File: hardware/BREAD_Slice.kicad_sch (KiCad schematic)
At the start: 15 parts, among them J1 Conn_01x10_Female, U1 AP63205

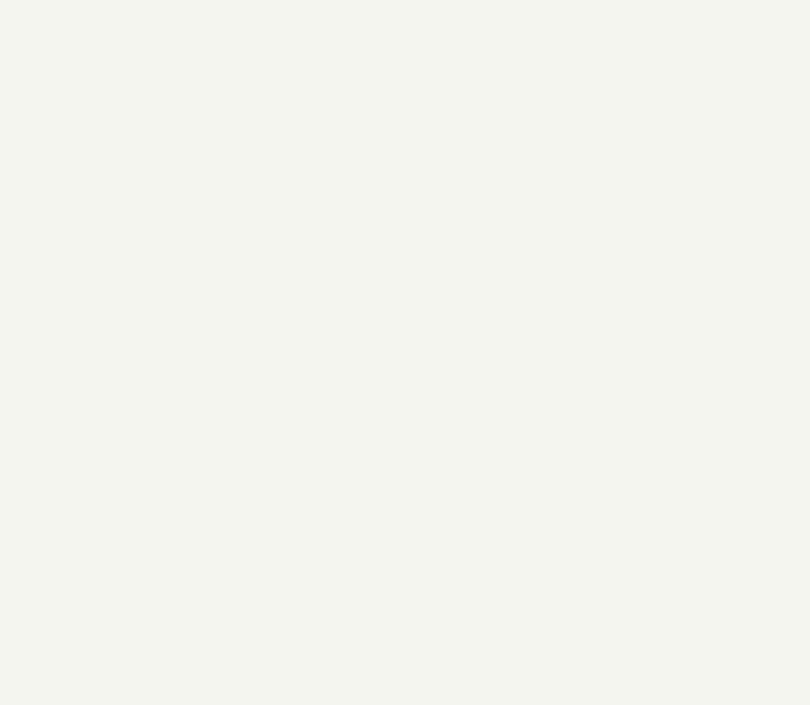
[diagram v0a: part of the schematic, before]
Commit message: initial commit, max31865 sub sheet done
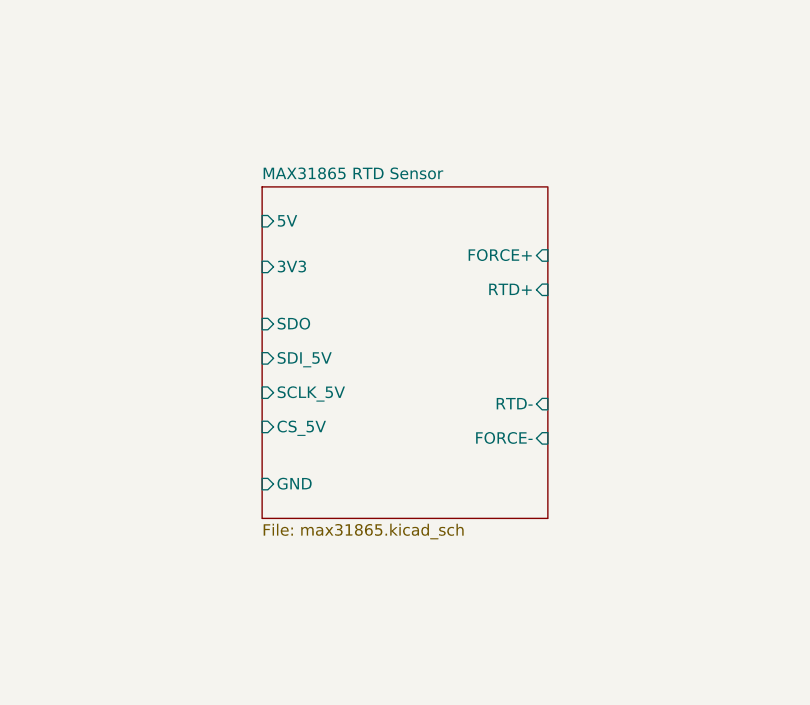
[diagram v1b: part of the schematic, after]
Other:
- added sheet MAX31865 RTD Sensor (max31865.kicad_sch)
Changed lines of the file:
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@@
 		(on_board yes)
 		(dnp no)
-		(property "Reference" "#FLG02"
+		(property "Reference" "#FLG03"
 			(at 48.895 49.53 0)
 			(effects
@@
 			(project "BREAD_Slice"
 				(path "/66043bca-a260-4915-9fce-8a51d324c687"
-					(reference "#FLG02")
+					(reference "#FLG03")
 					(unit 1)
 				)
@@
 		(on_board yes)
 		(dnp no)
-		(property "Reference" "#FLG01"
+		(property "Reference" "#FLG02"
 			(at 47.625 27.94 0)
 			(effects
@@
 			(project "BREAD_Slice"
 				(path "/66043bca-a260-4915-9fce-8a51d324c687"
-					(reference "#FLG01")
+					(reference "#FLG02")
 					(unit 1)
 				)
@@
 		(on_board yes)
 		(dnp no)
-		(property "Reference" "#PWR04"
+		(property "Reference" "#PWR02"
 			(at 26.67 95.25 0)
 			(effects
@@
 			(project "BREAD_Slice"
 				(path "/66043bca-a260-4915-9fce-8a51d324c687"
-					(reference "#PWR04")
+					(reference "#PWR02")
 					(unit 1)
 				)
@@
 		(on_board yes)
 		(dnp no)
-		(property "Reference" "#PWR02"
+		(property "Reference" "#PWR012"
 			(at 55.88 73.66 0)
 			(effects
@@
 			(project ""
 				(path "/66043bca-a260-4915-9fce-8a51d324c687"
-					(reference "#PWR02")
+					(reference "#PWR012")
 					(unit 1)
 				)
@@
 		(dnp no)
 		(fields_autoplaced yes)
-		(property "Reference" "#PWR05"
+		(property "Reference" "#PWR07"
 			(at 44.45 105.41 0)
 			(effects
@@
 			(project "BREAD_Slice"
 				(path "/66043bca-a260-4915-9fce-8a51d324c687"
-					(reference "#PWR05")
+					(reference "#PWR07")
 					(unit 1)
 				)
@@
 		(on_board yes)
 		(dnp no)
-		(property "Reference" "#PWR012"
+		(property "Reference" "#PWR08"
 			(at 45.72 119.38 0)
 			(effects
@@
 			(project "BREAD_Slice"
 				(path "/66043bca-a260-4915-9fce-8a51d324c687"
-					(reference "#PWR012")
+					(reference "#PWR08")
 					(unit 1)
 				)
@@
 		(on_board yes)
 		(dnp no)
-		(property "Reference" "#PWR08"
+		(property "Reference" "#PWR04"
 			(at 30.48 55.88 0)
 			(effects
@@
 			(project "BREAD_Slice"
 				(path "/66043bca-a260-4915-9fce-8a51d324c687"
-					(reference "#PWR08")
+					(reference "#PWR04")
 					(unit 1)
 				)
@@
 		(on_board yes)
 		(dnp no)
-		(property "Reference" "#PWR03"
+		(property "Reference" "#PWR09"
 			(at 46.99 95.25 0)
 			(effects
@@
 			(project ""
 				(path "/66043bca-a260-4915-9fce-8a51d324c687"
-					(reference "#PWR03")
+					(reference "#PWR09")
 					(unit 1)
 				)
@@
 		(on_board yes)
 		(dnp no)
-		(property "Reference" "#PWR09"
+		(property "Reference" "#PWR03"
 			(at 30.48 35.56 0)
 			(effects
@@
 			(project "BREAD_Slice"
 				(path "/66043bca-a260-4915-9fce-8a51d324c687"
-					(reference "#PWR09")
+					(reference "#PWR03")
 					(unit 1)
 				)
@@
 		(on_board yes)
 		(dnp no)
-		(property "Reference" "#FLG03"
+		(property "Reference" "#FLG01"
 			(at 28.575 100.33 0)
 			(effects
@@
 			(project "BREAD_Slice"
 				(path "/66043bca-a260-4915-9fce-8a51d324c687"
-					(reference "#FLG03")
+					(reference "#FLG01")
 					(unit 1)
 				)
@@
 		(on_board yes)
 		(dnp no)
-		(property "Reference" "#PWR07"
+		(property "Reference" "#PWR05"
 			(at 31.75 106.68 0)
 			(effects
@@
 			(project "BREAD_Slice"
 				(path "/66043bca-a260-4915-9fce-8a51d324c687"
-					(reference "#PWR07")
+					(reference "#PWR05")
 					(unit 1)
 				)
@@
 				)
 			)
+		)
+	)
+	(sheet
+		(at 123.19 55.88)
+		(size 31.75 36.83)
+		(exclude_from_sim no)
+		(in_bom yes)
+		(on_board yes)
+		(dnp no)
+		(fields_autoplaced yes)
+		(stroke
+			(width 0.1524)
+			(type solid)
+		)
+		(fill
+			(color 0 0 0 0.0000)
+		)
+		(property "Sheetname" "MAX31865 RTD Sensor"
+			(at 123.19 55.1684 0)
+			(effects
+				(font
+					(size 1.27 1.27)
+				)
+				(justify left bottom)
+			)
+		)
+		(property "Sheetfile" "max31865.kicad_sch"
+			(at 123.19 93.2946 0)
+			(effects
+				(font
+					(size 1.27 1.27)
+				)
+				(justify left top)
+			)
+		)
+		(pin "3V3" input
+			(at 123.19 64.77 180)
+			(effects
+				(font
+					(size 1.27 1.27)
+				)
+				(justify left)
+			)
+		)
+		(pin "5V" input
+			(at 123.19 59.69 180)
+			(effects
+				(font
+					(size 1.27 1.27)
+				)
+				(justify left)
+			)
+		)
+		(pin "CS_5V" input
+			(at 123.19 82.55 180)
+			(effects
+				(font
+					(size 1.27 1.27)
+				)
+				(justify left)
+			)
+		)
+		(pin "FORCE+" input
+			(at 154.94 63.5 0)
+			(effects
+				(font
+					(size 1.27 1.27)
+				)
+				(justify right)
+			)
+		)
+		(pin "FORCE-" input
+			(at 154.94 83.82 0)
+			(effects
+				(font
+					(size 1.27 1.27)
+				)
+				(justify right)
+			)
+		)
+		(pin "RTD+" input
+			(at 154.94 67.31 0)
+			(effects
+				(font
+					(size 1.27 1.27)
+				)
+				(justify right)
+			)
+		)
+		(pin "RTD-" input
+			(at 154.94 80.01 0)
+			(effects
+				(font
+					(size 1.27 1.27)
+				)
+				(justify right)
+			)
+		)
+		(pin "SCLK_5V" input
+			(at 123.19 78.74 180)
+			(effects
+				(font
+					(size 1.27 1.27)
+				)
+				(justify left)
+			)
+		)
+		(pin "SDI_5V" input
+			(at 123.19 74.93 180)
+			(effects
+				(font
+					(size 1.27 1.27)
+				)
+				(justify left)
+			)
+		)
+		(pin "SDO" input
+			(at 123.19 71.12 180)
+			(effects
+				(font
+					(size 1.27 1.27)
+				)
+				(justify left)
+			)
+		)
+		(pin "GND" input
+			(at 123.19 88.9 180)
+			(effects
+				(font
+					(size 1.27 1.27)
+				)
+				(justify left)
+			)
+		)
+		(instances
+			(project "BREAD_Slice"
+				(path "/66043bca-a260-4915-9fce-8a51d324c687"
+					(page "2")
+				)
+			)

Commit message: initial commit, complete schematic and board
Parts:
- added J2, J3, J4, J5, J6, J7, J8, J9: Screw_Terminal_01x02, TerminalBlock_4Ucon:TerminalBlock_4Ucon_1x02_P3.50mm_Horizontal, symbol Connector:Screw_Terminal_01x02
- added R1: 10k, Resistor_SMD:R_0805_2012Metric_Pad1.20x1.40mm_HandSolder, symbol Device:R
- added U2: TXB0108PW, Package_SO:TSSOP-20_4.4x6.5mm_P0.65mm, symbol Logic_LevelTranslator:TXB0108PW
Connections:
- net +5V: now also R1.1, U2.2 (V_{CCA})
- net GND: now also U2.1 (A1), U2.11 (GND)
- net MAX31865 RTD Sensor1/FORCE+: now also J2.2 (Pin_2)
- net MAX31865 RTD Sensor1/FORCE-: now also J3.1 (Pin_1)
- net MAX31865 RTD Sensor1/RTD+: now also J2.1 (Pin_1)
- net MAX31865 RTD Sensor1/RTD-: now also J3.2 (Pin_2)
- net CS4: now reaches A1.10 (D7)
- net CS4: now also U2.3 (A2)
- net CS3: now reaches A1.11 (D8)
- net CS3: now also U2.4 (A3)
- net CS2: now reaches A1.12 (D9)
- net CS2: now also U2.5 (A4)
- net CS1: now reaches A1.13 (D10)
- net CS1: now also U2.6 (A5)
- net MOSI: now reaches A1.14 (D11)
- net MOSI: now also U2.7 (A6)
- net MISO: now reaches A1.15 (D12)
- net MISO: now also U2.8 (A7)
- net SCK: now reaches A1.16 (D13)
- net SCK: now also U2.9 (A8)
- net +3.3V: now reaches A1.17 (3V3)
- net +3.3V: now also U2.19 (V_{CCB})
- net DRDY1: now reaches A1.19 (A0)
- net DRDY2: now reaches A1.20 (A1)
- net DRDY4: now reaches A1.21 (A2)
- net DRDY3: now reaches A1.22 (A3)
- new net: R1.2, U2.10 (OE)
- new net CS1_3V: U2.15 (B5)
- new net CS2_3V: U2.16 (B4)
- new net CS3_3V: U2.17 (B3)
- new net CS4_3V: U2.18 (B2)
- new net MAX31865 RTD Sensor2/FORCE+: J4.2 (Pin_2)
- new net MAX31865 RTD Sensor2/FORCE-: J5.1 (Pin_1)
- new net MAX31865 RTD Sensor2/RTD+: J4.1 (Pin_1)
- new net MAX31865 RTD Sensor2/RTD-: J5.2 (Pin_2)
- new net MAX31865 RTD Sensor3/FORCE+: J6.2 (Pin_2)
- new net MAX31865 RTD Sensor3/FORCE-: J7.1 (Pin_1)
- new net MAX31865 RTD Sensor3/RTD+: J6.1 (Pin_1)
- new net MAX31865 RTD Sensor3/RTD-: J7.2 (Pin_2)
- new net MAX31865 RTD Sensor4/FORCE+: J8.2 (Pin_2)
- new net MAX31865 RTD Sensor4/FORCE-: J9.1 (Pin_1)
- new net MAX31865 RTD Sensor4/RTD+: J8.1 (Pin_1)
- new net MAX31865 RTD Sensor4/RTD-: J9.2 (Pin_2)
- new net MISO_3V: U2.13 (B7)
- new net MOSI_3V: U2.14 (B6)
- new net SCK_3V: U2.12 (B8)
- no-connect marks 22 -> 11
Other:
- sheet MAX31865 RTD Sensor renamed MAX31865 RTD Sensor1
- added sheet MAX31865 RTD Sensor2 (max31865.kicad_sch)
- added sheet MAX31865 RTD Sensor3 (max31865.kicad_sch)
- added sheet MAX31865 RTD Sensor4 (max31865.kicad_sch)
- sheet MAX31865 RTD Sensor1 ports: added CS, DRDY, SCLK, SDI; removed 5V, CS_5V, SCLK_5V, SDI_5V

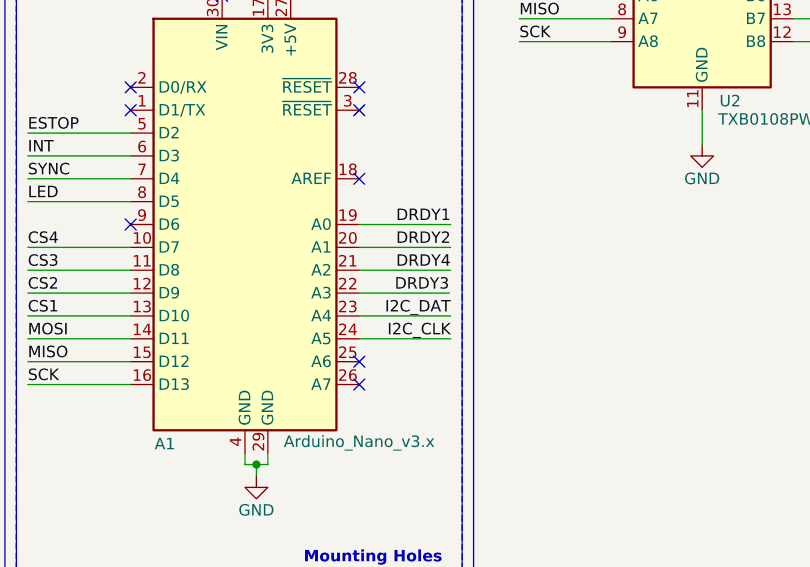
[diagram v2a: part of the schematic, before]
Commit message: review and revise board to use kmlib properly and clear drc/erc
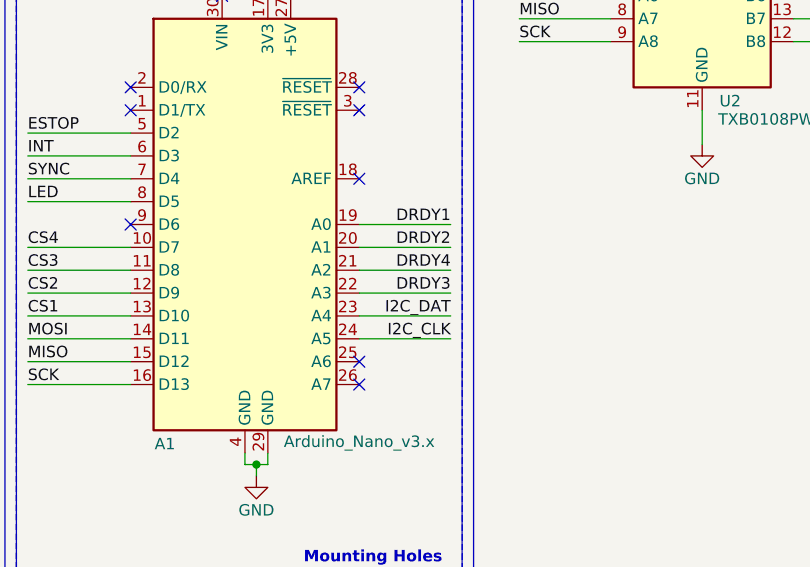
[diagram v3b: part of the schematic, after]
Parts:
- A1: footprint Module:Arduino_Nano -> KMLib_Boards_Modules:Arduino_Nano_Headers
- D1: footprint SparkFun-LED:WS2812-5050-4PIN -> KMLib_IC_SMD:WS2812-5050-4PIN; symbol SparkFun-LED:WS2812B_5050 -> KMLib_IC_Digital:WS2812B_5050_RGB_LED
- HS1: footprint kml-custom:Thermal Pad -> KMLib_Mounting:Thermal Pad
- J1: symbol Connector:Conn_01x10_Female -> Connector:Conn_01x10_Socket
- U1: footprint Package_TO_SOT_SMD:TSOT-23-6 -> KMLib_IC_SMD:SOIC_05WU-7_DIO; symbol SparkFun-DiscreteSemi:AP63205 -> KMLib_IC_Power:AP63205WU-7_Buck_Regulator
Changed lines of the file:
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@@
 	(wire
 		(pts
-			(xy 63.3413 151.13) (xy 53.34 151.13)
+			(xy 63.5 151.13) (xy 53.34 151.13)
 		)
 		(stroke
@@
 	)
 	(label "DRDY3"
-		(at 63.3413 151.13 180)
+		(at 63.5 151.13 180)
 		(effects
 			(font
@@
 			)
 		)
-		(property "Description" ""
+		(property "Description" "Mounting Hole without connection"
 			(at 49.53 185.42 0)
 			(effects
@@
 			)
 		)
-		(property "Description" ""
+		(property "Description" "Mounting Hole without connection"
 			(at 49.53 190.5 0)
 			(effects
@@
 			)
 		)
-		(property "Description" ""
+		(property "Description" "Mounting Hole without connection"
 			(at 57.15 185.42 0)
 			(effects
@@
 			)
 		)
-		(property "Description" ""
+		(property "Description" "Mounting Hole without connection"
 			(at 57.15 190.5 0)
 			(effects
@@
 			)
 		)
-		(property "Footprint" "Module:Arduino_Nano"
+		(property "Footprint" "KMLib_Boards_Modules:Arduino_Nano_Headers"
 			(at 40.64 143.51 0)
 			(effects
@@
 			)
 		)
-		(property "Description" ""
+		(property "Description" "Arduino Nano v3.x"
 			(at 40.64 143.51 0)
 			(effects
@@
 	)
 	(symbol
-		(lib_id "Connector:Conn_01x10_Female")
+		(lib_id "Connector:Conn_01x10_Socket")
 		(at 60.96 36.83 0)
 		(unit 1)
@@
 			)
 		)
-		(property "Description" ""
+		(property "Description" "Generic connector, single row, 01x10, script generated"
 			(at 60.96 36.83 0)
 			(effects
@@
 			)
 		)
-		(property "Description" ""
+		(property "Description" "Unpolarized capacitor, small symbol"
 			(at 52.07 72.39 0)
 			(effects
@@
 			)
 		)
-		(property "Description" ""
+		(property "Description" "Power symbol creates a global label with name \"+12V\""
 			(at 26.67 69.85 0)
 			(effects
@@
 			)
 		)
-		(property "Description" ""
+		(property "Description" "Unpolarized capacitor, small symbol"
 			(at 52.07 82.55 0)
 			(effects
@@
 	)
 	(symbol
-		(lib_id "SparkFun-DiscreteSemi:AP63205")
+		(lib_id "KMLib_IC_Power:AP63205WU-7_Buck_Regulator")
 		(at 35.56 73.66 0)
 		(unit 1)
@@
 			)
 		)
-		(property "Footprint" "Package_TO_SOT_SMD:TSOT-23-6"
+		(property "Footprint" "KMLib_IC_SMD:SOIC_05WU-7_DIO"
 			(at 35.56 73.66 0)
 			(effects
@@
 	)
 	(symbol
-		(lib_name "WS2812B_5050_1")
-		(lib_id "SparkFun-LED:WS2812B_5050")
+		(lib_id "KMLib_IC_Digital:WS2812B_5050_RGB_LED")
 		(at 30.48 40.64 0)
 		(unit 1)
@@
 			)
 		)
-		(property "Footprint" "SparkFun-LED:WS2812-5050-4PIN"
+		(property "Footprint" "KMLib_IC_SMD:WS2812-5050-4PIN"
 			(at 13.97 49.53 0)
 			(effects
@@
 	)
 	(symbol
-		(lib_name "+12V_1")
 		(lib_id "power:+12V")
 		(at 53.34 27.94 0)
@@
 			)
 		)
-		(property "Footprint" "kml-custom:Thermal Pad"
+		(property "Footprint" "KMLib_Mounting:Thermal Pad"
 			(at 35.8648 97.79 0)
 			(effects
@@
 			)
 		)
-		(property "Description" ""
+		(property "Description" "Inductor, small symbol"
 			(at 52.07 77.47 0)
 			(effects
@@
 			)
 		)
-		(property "Description" ""
+		(property "Description" "Unpolarized capacitor, small symbol"
 			(at 62.23 82.55 0)
 			(effects
@@
 			)
 		)
-		(property "Description" ""
+		(property "Description" "Unpolarized capacitor, small symbol"
 			(at 26.67 80.01 0)
 			(effects
